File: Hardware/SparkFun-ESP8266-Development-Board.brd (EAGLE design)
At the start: 55.9 x 25.9 mm, 73 parts, among them J1 DNP, Q1 2.5A/30V, U1 ESP8266, U2 MCP73831, U3 AT25SF041-SOIC8, U4 AP2112K-3.3V, U5 ATECC108-MAHDA, U6 TMP1021:1, U7 TSL2561FN, Y1 26MHz

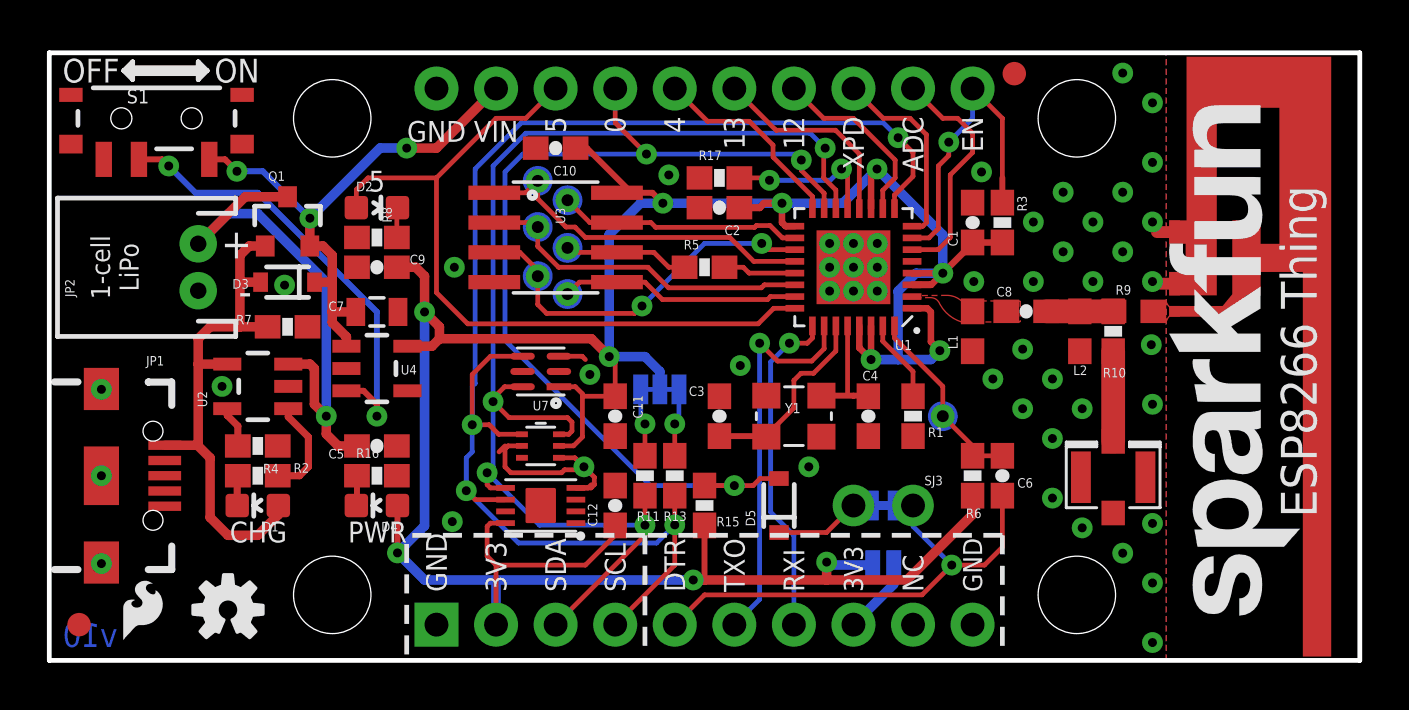
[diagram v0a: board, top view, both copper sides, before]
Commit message: Bringing board width down to 2.18 inches.
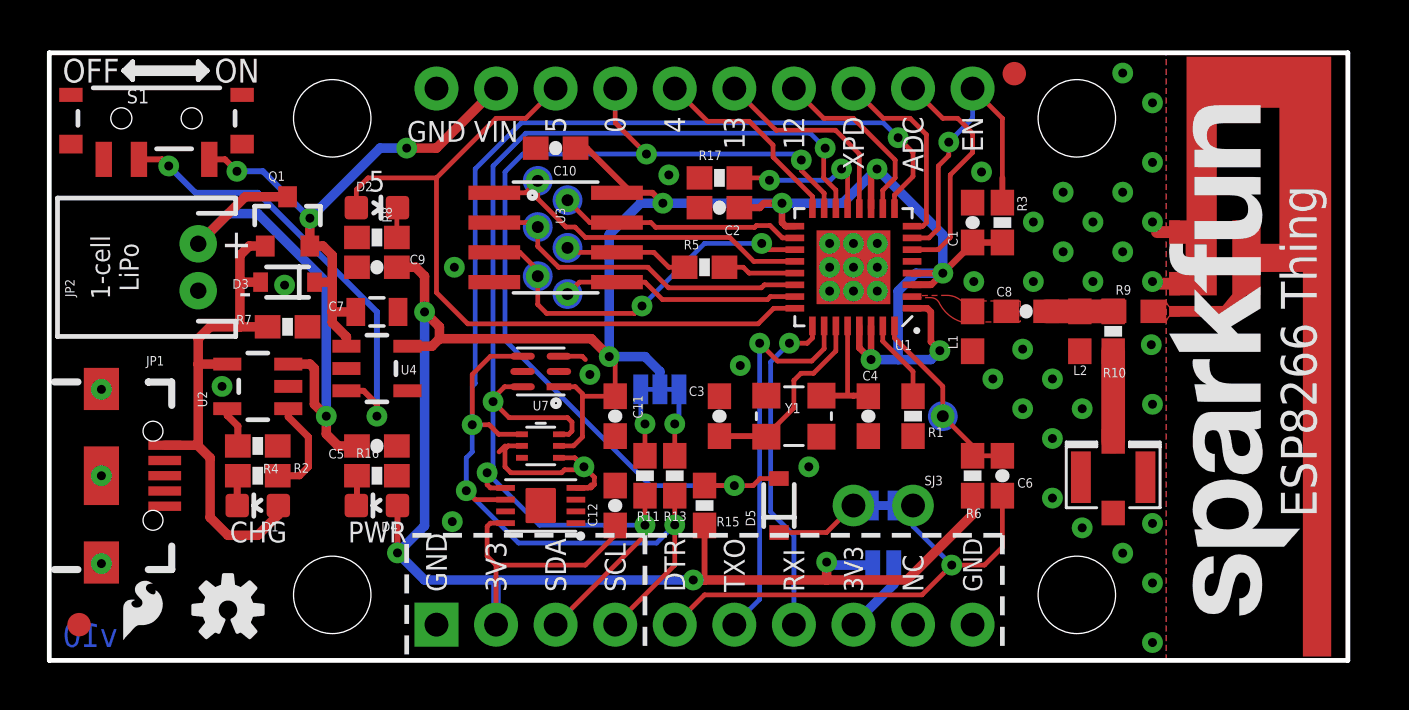
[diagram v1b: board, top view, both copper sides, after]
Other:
- board size 55.9 x 25.9 mm -> 55.4 x 25.9 mm

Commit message: Revising TMP102, ATECC108 & TSL2561 to DNP. Moving dimensions to correct layer.
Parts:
- C11, C12: value 0.1uF -> DNP
- U5: value ATECC108-MAHDA -> DNP
- U6: value TMP1021:1 -> DNP
- U7: value TSL2561FN -> DNP
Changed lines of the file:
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@@
 <layer number="47" name="Measures" color="7" fill="1" visible="no" active="yes"/>
 <layer number="48" name="Document" color="7" fill="1" visible="no" active="yes"/>
-<layer number="49" name="Reference" color="7" fill="1" visible="yes" active="yes"/>
+<layer number="49" name="Reference" color="7" fill="1" visible="no" active="yes"/>
 <layer number="50" name="dxf" color="7" fill="1" visible="no" active="no"/>
 <layer number="51" name="tDocu" color="6" fill="1" visible="yes" active="yes"/>
@@
 <text x="22.733" y="17.3355" size="0.8636" layer="22" font="vector" ratio="15" rot="MR0" align="center-right">CLK</text>
 <text x="22.733" y="15.367" size="0.8636" layer="22" font="vector" ratio="15" rot="MR0" align="center-right">SI</text>
-<dimension x1="0" y1="-0.254" x2="0" y2="25.654" x3="-7.874" y3="12.7" textsize="0.8636" textratio="15" layer="49" unit="inch"/>
-<dimension x1="0" y1="-0.254" x2="55.372" y2="-0.254" x3="27.686" y3="-6.35" textsize="0.8636" textratio="15" layer="49" unit="inch"/>
-<dimension x1="10.16" y1="2.54" x2="10.16" y2="-0.254" x3="-2.54" y3="1.143" textsize="0.8636" textratio="15" layer="49" unit="inch"/>
-<dimension x1="12.065" y1="2.54" x2="0" y2="2.54" x3="6.0325" y3="-2.286" textsize="0.8636" textratio="15" layer="49" unit="inch" precision="3"/>
-<dimension x1="12.065" y1="22.86" x2="0" y2="22.86" x3="6.0325" y3="28.956" textsize="0.8636" textratio="15" layer="49" unit="inch" precision="3"/>
-<dimension x1="10.16" y1="22.86" x2="10.16" y2="-0.254" x3="-4.572" y3="11.303" textsize="0.8636" textratio="15" layer="49" unit="inch"/>
-<dimension x1="16.51" y1="1.27" x2="16.51" y2="-0.254" x3="-0.508" y3="0.508" textsize="0.8636" textratio="15" layer="49" unit="inch"/>
-<dimension x1="16.51" y1="24.13" x2="16.51" y2="-0.254" x3="-6.096" y3="11.938" textsize="0.8636" textratio="15" layer="49" unit="inch"/>
-<dimension x1="16.51" y1="1.27" x2="0" y2="1.27" x3="8.255" y3="-4.318" textsize="0.8636" textratio="15" layer="49" unit="inch"/>
-<dimension x1="16.51" y1="1.27" x2="19.05" y2="1.27" x3="17.78" y3="-1.778" textsize="0.8636" textratio="15" layer="49" unit="inch"/>
-<dimension x1="16.51" y1="24.13" x2="0" y2="24.13" x3="8.255" y3="26.924" textsize="0.8636" textratio="15" layer="49" unit="inch"/>
-<dimension x1="43.815" y1="22.86" x2="0" y2="22.86" x3="21.9075" y3="30.988" textsize="0.8636" textratio="15" layer="49" unit="inch" precision="3"/>
-<dimension x1="43.815" y1="22.86" x2="45.466" y2="22.86" x3="44.6405" y3="27.686" textsize="0.8636" textratio="15" layer="49" unit="inch" precision="3"/>
+<dimension x1="0" y1="-0.254" x2="0" y2="25.654" x3="-7.874" y3="12.7" textsize="0.8636" textratio="15" layer="47" unit="inch"/>
+<dimension x1="0" y1="-0.254" x2="55.372" y2="-0.254" x3="27.686" y3="-6.35" textsize="0.8636" textratio="15" layer="47" unit="inch"/>
+<dimension x1="10.16" y1="2.54" x2="10.16" y2="-0.254" x3="-2.54" y3="1.143" textsize="0.8636" textratio="15" layer="47" unit="inch"/>
+<dimension x1="12.065" y1="2.54" x2="0" y2="2.54" x3="6.0325" y3="-2.286" textsize="0.8636" textratio="15" layer="47" unit="inch" precision="3"/>
+<dimension x1="12.065" y1="22.86" x2="0" y2="22.86" x3="6.0325" y3="28.956" textsize="0.8636" textratio="15" layer="47" unit="inch" precision="3"/>
+<dimension x1="10.16" y1="22.86" x2="10.16" y2="-0.254" x3="-4.572" y3="11.303" textsize="0.8636" textratio="15" layer="47" unit="inch"/>
+<dimension x1="16.51" y1="1.27" x2="16.51" y2="-0.254" x3="-0.508" y3="0.508" textsize="0.8636" textratio="15" layer="47" unit="inch"/>
+<dimension x1="16.51" y1="24.13" x2="16.51" y2="-0.254" x3="-6.096" y3="11.938" textsize="0.8636" textratio="15" layer="47" unit="inch"/>
+<dimension x1="16.51" y1="1.27" x2="0" y2="1.27" x3="8.255" y3="-4.318" textsize="0.8636" textratio="15" layer="47" unit="inch"/>
+<dimension x1="16.51" y1="1.27" x2="19.05" y2="1.27" x3="17.78" y3="-1.778" textsize="0.8636" textratio="15" layer="47" unit="inch"/>
+<dimension x1="16.51" y1="24.13" x2="0" y2="24.13" x3="8.255" y3="26.924" textsize="0.8636" textratio="15" layer="47" unit="inch"/>
+<dimension x1="43.815" y1="22.86" x2="0" y2="22.86" x3="21.9075" y3="30.988" textsize="0.8636" textratio="15" layer="47" unit="inch" precision="3"/>
+<dimension x1="43.815" y1="22.86" x2="45.466" y2="22.86" x3="44.6405" y3="27.686" textsize="0.8636" textratio="15" layer="47" unit="inch" precision="3"/>
 <text x="8.9154" y="5.6642" size="0.889" layer="21" font="vector" ratio="15" rot="R180" align="bottom-center">CHG</text>
 <text x="8.636" y="17.526" size="1.27" layer="21" font="vector" ratio="15" align="center-right">+</text>
@@
 </element>
 <element name="U3" library="esp8266-development-board" package="SO08" value="AT25SF041-SOIC8" x="21.59" y="17.78" rot="R270"/>
-<element name="U5" library="esp8266-development-board" package="UDFN8" value="ATECC108-MAHDA" x="20.955" y="6.35" rot="R180"/>
+<element name="U5" library="esp8266-development-board" package="UDFN8" value="DNP" x="20.955" y="6.35" rot="R180"/>
 <element name="R13" library="SparkFun-Resistors" package="0603-RES" value="2.2k" x="26.67" y="7.62" smashed="yes" rot="R90">
 <attribute name="PROD_ID" value="RES-08272" x="26.67" y="7.62" size="1.778" layer="27" font="vector" ratio="15" rot="R90" display="off"/>
@@
 <attribute name="PROD_ID" value="CAP-00810" x="21.59" y="21.59" size="1.016" layer="27" font="vector" ratio="15" rot="R180" display="off"/>
 </element>
-<element name="C11" library="SparkFun-Capacitors" package="0603-CAP" value="0.1uF" x="24.13" y="10.16" rot="R270">
+<element name="C11" library="SparkFun-Capacitors" package="0603-CAP" value="DNP" x="24.13" y="10.16" rot="R270">
 <attribute name="PROD_ID" value="CAP-00810" x="24.13" y="10.16" size="1.016" layer="27" font="vector" ratio="15" rot="R270" display="off"/>
 </element>
@@
 <attribute name="PROD_ID" value="RES-00824" x="28.575" y="20.32" size="1.778" layer="27" font="vector" ratio="15" display="off"/>
 </element>
-<element name="U6" library="SparkFun-Sensors" package="SOT563-2" value="TMP1021:1" x="20.955" y="8.89"/>
+<element name="U6" library="SparkFun-Sensors" package="SOT563-2" value="DNP" x="20.955" y="8.89"/>
 <element name="D5" library="SparkFun-DiscreteSemi" package="SOD-323" value="" x="31.115" y="6.35" rot="R90">
 <attribute name="PROD_ID" value="DIO-09646" x="31.115" y="6.35" size="1.778" layer="27" font="vector" ratio="15" rot="R90" display="off"/>
@@
 <element name="SJ3" library="SparkFun-Passives" package="PTH-JUMPER-NC_BOTTOM_NO_SILK" value="" x="35.56" y="6.35" rot="R180"/>
 <element name="LOGO5" library="SparkFun-Aesthetics" package="SFE_LOGO_NAME_.2" value="SFE_LOGO_NAME.2_INCH" x="53.34" y="1.651" rot="R90"/>
-<element name="U7" library="esp8266-development-board" package="FN-6" value="TSL2561FN" x="20.955" y="12.065" rot="R180"/>
-<element name="C12" library="SparkFun-Capacitors" package="0603-CAP" value="0.1uF" x="24.13" y="6.35" rot="R90">
+<element name="U7" library="esp8266-development-board" package="FN-6" value="DNP" x="20.955" y="12.065" rot="R180"/>
+<element name="C12" library="SparkFun-Capacitors" package="0603-CAP" value="DNP" x="24.13" y="6.35" rot="R90">
 <attribute name="PROD_ID" value="CAP-00810" x="24.13" y="6.35" size="0.8128" layer="27" font="vector" ratio="15" rot="R90" display="off"/>
 </element>
